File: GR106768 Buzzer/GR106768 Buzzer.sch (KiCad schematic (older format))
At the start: 0 parts

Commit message: Adding first pass at Buzzer Board schematic
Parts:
- added BZ1, BZ2: PKM33, symbol Device:Buzzer
- added C1: 47pF, symbol c_network:C_NETWORK
- added C10, C11, C30, C5, C7, C8, C9: 100nF, symbol Device:C
- added C12: 470μF, symbol Device:CP
- added C13, C14: 33nF, symbol Device:C
- added C2: 220pF, symbol Device:C
- added C3: 10nF, symbol Device:C
- added C4, C6: 680pF, symbol Device:C
- added D1: NC, symbol Device:D_Zener
- added D2: BAT54C, Package_TO_SOT_SMD:SOT-23, symbol Diode:BAT54C
- added D3, D4: BAT54S, Package_TO_SOT_SMD:SOT-23, symbol Diode:BAT54S
- added D5: BZX84C2V7, symbol Device:D_Zener
- added F1: 500mA, symbol Device:Fuse
- added FI1: BLA31BD221SN4D, FB_BLA31BD221SN4D, symbol bla31bd:BLA31BD221SN4D
- added J1: Conn_01x07, symbol Connector_Generic:Conn_01x07
- added L1: Core_Ferrite, symbol Device:L_Core_Ferrite
- added Q1, Q2: BC847, Package_TO_SOT_SMD:SOT-23, symbol Transistor_BJT:BC847
- added Q3, Q4: BC857, Package_TO_SOT_SMD:SOT-23, symbol Transistor_BJT:BC857
- added R1, R10, R2, R24, R29, R3, R59: 100k, symbol Device:R
- added R11: 105k, symbol Device:R
- added R12, R22: 470, symbol Device:R
- added R13, R14, R19, R20: 1.5, symbol Device:R
- added R15: 33, symbol Device:R
- added R16, R17, R4, R5: 10k, symbol Device:R
- added R18, R21: 150k, symbol Device:R
- added R23: 2.2K, symbol Device:R
- added R25: NC, symbol Device:R
- added R26: 137k, symbol Device:R
- added R27: 68k, symbol Device:R
- added R28, R9: 32.4k, symbol Device:R
- added R6: 50k, symbol Device:R
- added R69: 200k, symbol Device:R
- added R7: 51.1k, symbol Device:R
- added R8: 1k, symbol Device:R
- added U1, U2: MC33172, symbol Amplifier_Operational:LM358
- added U3: LMC7211, symbol lmc7211:LMC7211
- added U4: LMV321, symbol Amplifier_Operational:LMV321
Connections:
- net labels added: +12V, +5V, -12V, BUZ_ACT, GND, INHIB_STOP_INV, STOP_INV, SUPPLY_BUZ, TESTBUZ, TEST_BUZZER, VBAT, VCHARG
- wire segments 0 -> 244
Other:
- note added: "+5V_CPU"
- note added: "GND"
- note added: "INHIB-STOP-INV-CPU"
- note added: "PWM-BUZZER-CPU"
- note added: "STOP-INV-CPU"
- note added: "SUPPLY-BUZ-CPU"
- note added: "TEST-BUZZER-CPU"

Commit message: Changed global nets to hierarchical
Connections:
- net labels removed: TESTBUZ
- wire segments 244 -> 250
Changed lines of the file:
@@
 EESchema Schematic File Version 4
-LIBS:GR106768 Buzzer-cache
 EELAYER 30 0
 EELAYER END
@@
 	1    0    0    -1
 $EndComp
-Text GLabel 4700 4250 0    50   Input ~ 0
-SUPPLY_BUZ
 $Comp
 L Device:C C10
@@
 	0    -1   -1   0
 $EndComp
-Text GLabel 4325 2600 2    50   Input ~ 0
-TEST_BUZZER
-Text GLabel 4325 2750 2    50   Output ~ 0
-STOP_INV
 $Comp
 L Diode:BAT54S D4
@@
 	1    0    0    -1
 $EndComp
-Text GLabel 14525 6200 2    50   Output ~ 0
-TESTBUZ
-Text GLabel 12775 6975 0    50   Input ~ 0
-VBAT
-Text GLabel 12600 6075 0    50   Output ~ 0
-BUZ_ACT
 $Comp
 L Device:C C30
@@
 Wire Wire Line
 	13300 6975 13300 7050
-Text GLabel 13925 6975 2    50   Input ~ 0
-VCHARG
 Wire Wire Line
 	13925 6975 13700 6975
@@
 Wire Wire Line
 	2350 2800 2300 2800
-Text GLabel 4325 2450 2    50   Output ~ 0
-INHIB_STOP_INV
 Wire Wire Line
 	3175 2300 4325 2300
-Text GLabel 4325 2300 2    50   Input ~ 0
-SUPPLY_BUZ
 Wire Wire Line
 	6425 2900 5950 2900
@@
 Wire Wire Line
 	3750 6250 3750 6350
-$Sheet
-S 2450 7725 1200 900
-U 5E89C6B8
-F0 "GR106768_buzzer_charger" 50
-F1 "GR106768_buzzer_charger.sch" 50
-$EndSheet
 Wire Wire Line
 	7900 4450 13950 4450
@@
 	4250 2900 5025 2900
 Connection ~ 5025 2900
+Wire Wire Line
+	3650 7925 3825 7925
+Text HLabel 3825 7925 2    50   Output ~ 0
+SUPPLY_BUZ
+$Sheet
+S 2450 7725 1200 900
+U 5E89C6B8
+F0 "GR106768_buzzer_charger" 50
+F1 "GR106768_buzzer_charger.sch" 50
+F2 "BUZ_ACT" I L 2450 7925 50
+F3 "SUPPLY_BUZ" O R 3650 7925 50
+F4 "STOP_INV" I L 2450 8025 50
+F5 "INHIB_STOP_INV" I L 2450 8125 50
+F6 "VBAT" O R 3650 8025 50
+F7 "VCHARG" O R 3650 8125 50
+$EndSheet
+Wire Wire Line
+	2300 8125 2450 8125
+Wire Wire Line
+	2300 8025 2450 8025
+Wire Wire Line
+	2300 7925 2450 7925
+Text HLabel 2300 7925 0    50   Input ~ 0
+BUZ_ACT
+Text HLabel 2300 8025 0    50   Input ~ 0
+STOP_INV
+Text HLabel 2300 8125 0    50   Input ~ 0
+INHIB_STOP_INV
+Text HLabel 3825 8125 2    50   Output ~ 0
+VCHARG
+Wire Wire Line
+	3650 8025 3825 8025
+Text HLabel 3825 8025 2    50   Output ~ 0
+VBAT
+Text HLabel 12775 6975 0    50   Input ~ 0
+VBAT
+Text HLabel 12600 6075 0    50   Output ~ 0
+BUZ_ACT
+Text HLabel 4700 4250 0    50   Input ~ 0
+SUPPLY_BUZ
+Text HLabel 4325 2750 2    50   Output ~ 0
+STOP_INV
+Text HLabel 14525 6200 2    50   Output ~ 0
+TEST_BUZZER
+Text HLabel 4325 2600 2    50   Input ~ 0
+TEST_BUZZER
+Text HLabel 4325 2450 2    50   Output ~ 0
+INHIB_STOP_INV
+Text HLabel 4325 2300 2    50   Input ~ 0
+SUPPLY_BUZ
+Wire Wire Line
+	3650 8125 3825 8125
+Text HLabel 13925 6975 2    50   Input ~ 0
+VCHARG
 $EndSCHEMATC

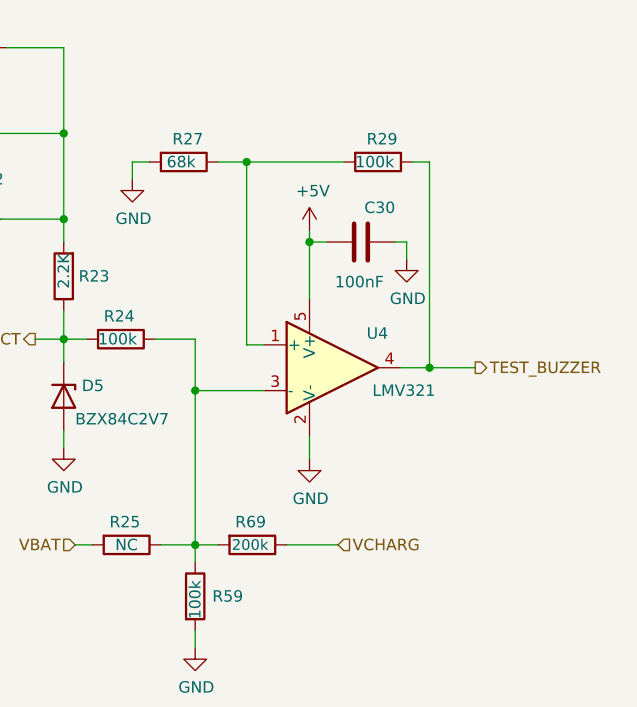
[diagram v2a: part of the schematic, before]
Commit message: Fixed U4 pins (KiCad part is different)
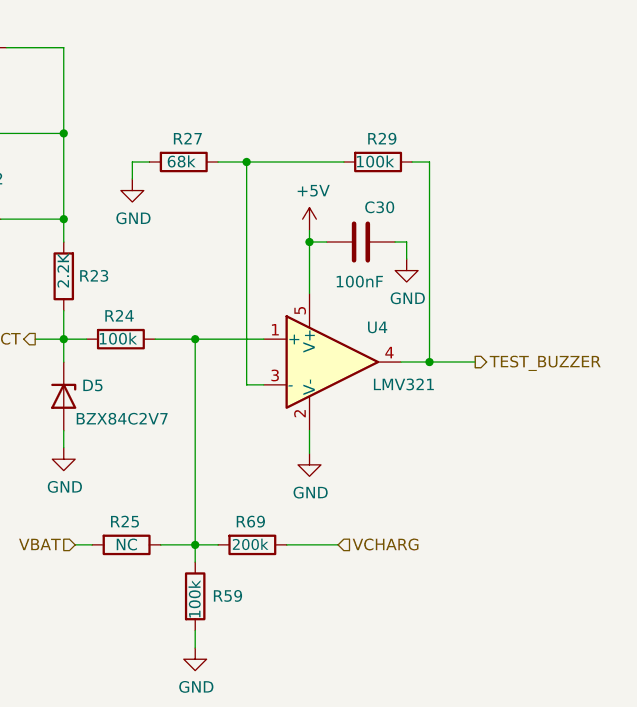
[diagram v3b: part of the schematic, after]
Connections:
- wire segments 250 -> 249
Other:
- moved on the sheet: U4
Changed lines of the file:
@@
 	10400 3325 10400 3125
-$Comp
-L Amplifier_Operational:LMV321 U4
-U 1 1 5E9F6105
-P 13900 6200
-F 0 "U4" H 14050 6350 50  0000 L CNN
-F 1 "LMV321" H 14075 6100 50  0000 L CNN
-F 2 "" H 13900 6200 50  0001 L CNN
-F 3 "http://www.ti.com/lit/ds/symlink/lmv324.pdf" H 13900 6200 50  0001 C CNN
-	1    13900 6200
-	1    0    0    -1
-$EndComp
-$Comp
-L power:GND #PWR027
-U 1 1 5E9F8A01
-P 13800 6600
-F 0 "#PWR027" H 13800 6350 50  0001 C CNN
-F 1 "GND" H 13805 6427 50  0000 C CNN
-F 2 "" H 13800 6600 50  0001 C CNN
-F 3 "" H 13800 6600 50  0001 C CNN
-	1    13800 6600
-	1    0    0    -1
-$EndComp
 $Comp
 L Device:C C30
@@
 $EndComp
 $Comp
-L power:GND #PWR021
-U 1 1 5EA0E815
-P 14225 5725
-F 0 "#PWR021" H 14225 5475 50  0001 C CNN
-F 1 "GND" H 14230 5552 50  0000 C CNN
-F 2 "" H 14225 5725 50  0001 C CNN
-F 3 "" H 14225 5725 50  0001 C CNN
-	1    14225 5725
-	1    0    0    -1
-$EndComp
-$Comp
 L Device:R R69
 U 1 1 5EA111CA
@@
 $EndComp
 Wire Wire Line
-	14200 6200 14325 6200
-Wire Wire Line
 	13875 5650 13800 5650
 Wire Wire Line
-	13800 5650 13800 5900
-Wire Wire Line
 	14175 5650 14225 5650
-Wire Wire Line
-	14225 5650 14225 5725
 $Comp
 L power:+5V #PWR018
@@
 $EndComp
 Wire Wire Line
-	13800 5600 13800 5650
-Connection ~ 13800 5650
-Wire Wire Line
-	14325 5300 14325 6200
-Connection ~ 14325 6200
-Wire Wire Line
-	14325 6200 14525 6200
-Wire Wire Line
 	14250 5300 14325 5300
 Wire Wire Line
 	13950 5300 13525 5300
-Wire Wire Line
-	13600 6100 13525 6100
-Wire Wire Line
-	13525 6100 13525 5300
 Connection ~ 13525 5300
 Wire Wire Line
@@
 Wire Wire Line
 	13025 5300 13025 5375
-Wire Wire Line
-	13800 6600 13800 6500
 Wire Wire Line
 	12775 6975 12850 6975
@@
 Connection ~ 13300 6975
 Wire Wire Line
-	13600 6300 13300 6300
-Wire Wire Line
-	13300 6300 13300 6975
-Wire Wire Line
 	13125 6075 13300 6075
-Wire Wire Line
-	13300 6075 13300 6300
-Connection ~ 13300 6300
 $Comp
 L power:GND #PWR026
@@
 Text HLabel 4325 2750 2    50   Output ~ 0
 STOP_INV
-Text HLabel 14525 6200 2    50   Output ~ 0
-TEST_BUZZER
 Text HLabel 4325 2600 2    50   Input ~ 0
 TEST_BUZZER
@@
 Text HLabel 13925 6975 2    50   Input ~ 0
 VCHARG
+Wire Wire Line
+	14225 5650 14225 5725
+Text HLabel 14525 6175 2    50   Output ~ 0
+TEST_BUZZER
+Wire Wire Line
+	13800 6575 13800 6475
+Wire Wire Line
+	14325 5300 14325 6175
+$Comp
+L power:GND #PWR021
+U 1 1 5EA0E815
+P 14225 5725
+F 0 "#PWR021" H 14225 5475 50  0001 C CNN
+F 1 "GND" H 14230 5552 50  0000 C CNN
+F 2 "" H 14225 5725 50  0001 C CNN
+F 3 "" H 14225 5725 50  0001 C CNN
+	1    14225 5725
+	1    0    0    -1
+$EndComp
+$Comp
+L power:GND #PWR027
+U 1 1 5E9F8A01
+P 13800 6575
+F 0 "#PWR027" H 13800 6325 50  0001 C CNN
+F 1 "GND" H 13805 6402 50  0000 C CNN
+F 2 "" H 13800 6575 50  0001 C CNN
+F 3 "" H 13800 6575 50  0001 C CNN
+	1    13800 6575
+	1    0    0    -1
+$EndComp
+$Comp
+L Amplifier_Operational:LMV321 U4
+U 1 1 5E9F6105
+P 13900 6175
+F 0 "U4" H 14050 6325 50  0000 L CNN
+F 1 "LMV321" H 14075 6075 50  0000 L CNN
+F 2 "" H 13900 6175 50  0001 L CNN
+F 3 "http://www.ti.com/lit/ds/symlink/lmv324.pdf" H 13900 6175 50  0001 C CNN
+	1    13900 6175
+	1    0    0    -1
+$EndComp
+Wire Wire Line
+	13300 6075 13300 6975
+Wire Wire Line
+	13300 6075 13600 6075
+Connection ~ 13300 6075
+Wire Wire Line
+	13525 6275 13600 6275
+Wire Wire Line
+	13525 5300 13525 6275
+Wire Wire Line
+	13800 5600 13800 5650
+Wire Wire Line
+	13800 5875 13800 5650
+Connection ~ 13800 5650
+Connection ~ 14325 6175
+Wire Wire Line
+	14325 6175 14525 6175
+Wire Wire Line
+	14200 6175 14325 6175
 $EndSCHEMATC

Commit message: Merged Buzzer libraries into master library
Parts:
- removed C1: 47pF, symbol c_network:C_NETWORK
- removed FI1: BLA31BD221SN4D, FB_BLA31BD221SN4D, symbol bla31bd:BLA31BD221SN4D
- removed U3: LMC7211, symbol lmc7211:LMC7211
- added C1: 47pF, symbol GR106768~Buzzer:C_NETWORK
- added FI1: BLA31BD221SN4D, FB_BLA31BD221SN4D, symbol GR106768~Buzzer:BLA31BD221SN4D
- added U3: LMC7211, symbol GR106768~Buzzer:LMC7211
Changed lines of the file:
@@
-$EndComp
-$Comp
-L lmc7211:LMC7211 U3
-U 1 1 5E8BBAEB
-P 5900 4850
-F 0 "U3" H 5950 5150 50  0000 L CNN
-F 1 "LMC7211" H 5950 4575 50  0000 L CNN
-F 2 "" H 5700 4850 50  0001 C CNN
-F 3 "" H 5700 4850 50  0001 C CNN
-	1    5900 4850
-	1    0    0    -1
 $EndComp
 $Comp
@@
 Wire Wire Line
 	8950 3500 9175 3500
-$Comp
-L bla31bd:BLA31BD221SN4D FI1
-U 1 1 5E8BD79C
-P 3950 2700
-F 0 "FI1" H 3950 3175 50  0000 C CNN
-F 1 "BLA31BD221SN4D" H 3950 2325 50  0000 C CNN
-F 2 "FB_BLA31BD221SN4D" H 3950 2700 50  0001 L BNN
-F 3 "1206 Murata" H 3950 2700 50  0001 L BNN
-F 4 "1mm" H 3950 2700 50  0001 L BNN "Champ4"
-F 5 "Murata Electronics" H 3950 2700 50  0001 L BNN "Champ5"
-F 6 "None" H 3950 2700 50  0001 L BNN "Champ6"
-F 7 "Manufacturer recommendations" H 3950 2700 50  0001 L BNN "Champ7"
-F 8 "Unavailable" H 3950 2700 50  0001 L BNN "Champ8"
-F 9 "Ferrite Beads Chip Bead Array 1KOhm 25% 100MHz 50mA 1206 Paper T/R" H 3950 2700 50  0001 L BNN "Champ9"
-F 10 "JENF243A–0008N-01" H 3950 2700 50  0001 L BNN "Champ10"
-F 11 "BLA31AG102SN4D" H 3950 2700 50  0001 L BNN "Champ11"
-	1    3950 2700
-	1    0    0    -1
-$EndComp
 Wire Wire Line
 	4250 2600 4325 2600
@@
 Wire Wire Line
 	3125 2500 3125 2750
-$Comp
-L c_network:C_NETWORK C1
-U 1 1 5E8870D5
-P 3225 4000
-F 0 "C1" H 3625 4175 50  0000 L CNN
-F 1 "47pF" H 3625 3825 50  0000 L CNN
-F 2 "" H 2963 3850 50  0001 C CNN
-F 3 "~" H 2925 4000 50  0001 C CNN
-	1    3225 4000
-	1    0    0    -1
-$EndComp
 Wire Wire Line
 	2925 2900 2925 3800
@@
 Wire Wire Line
 	14200 6175 14325 6175
+$Comp
+L GR106768~Buzzer:BLA31BD221SN4D FI1
+U 1 1 5FB00CBD
+P 3950 2700
+F 0 "FI1" H 3950 3150 50  0000 C CNN
+F 1 "BLA31BD221SN4D" H 3950 2350 50  0000 C CNN
+F 2 "FB_BLA31BD221SN4D" H 3550 2200 50  0001 L BNN
+F 3 "1206 Murata" H 3650 1650 50  0001 L BNN
+F 4 "Murata Electronics" H 3600 2100 50  0001 L BNN "Champ5"
+	1    3950 2700
+	1    0    0    -1
+$EndComp
+$Comp
+L GR106768~Buzzer:C_NETWORK C1
+U 1 1 5FB0366D
+P 3225 4000
+F 0 "C1" H 3678 4059 50  0000 L CNN
+F 1 "47pF" H 3678 3968 50  0000 L CNN
+F 2 "" H 2963 3850 50  0001 C CNN
+F 3 "~" H 2925 4000 50  0001 C CNN
+	1    3225 4000
+	1    0    0    -1
+$EndComp
+$Comp
+L GR106768~Buzzer:LMC7211 U3
+U 1 1 5FB0685F
+P 5900 4850
+F 0 "U3" H 5975 5100 50  0000 L CNN
+F 1 "LMC7211" H 5975 4575 50  0000 L CNN
+F 2 "" H 5700 4850 50  0001 C CNN
+F 3 "" H 5700 4850 50  0001 C CNN
+	1    5900 4850
+	1    0    0    -1
+$EndComp
 $EndSCHEMATC

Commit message: Updating Buzzer and start of board
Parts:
- BZ1, BZ2: footprint (none) -> footprint_buzzer:Buzzer_Murata_PKM33EPH1201C
- C1: footprint (none) -> footprint_buzzer:CA0612KRX7R9BB102
- C10, C11, C12, C13, C14, C2, C3, C30, C4, C5, C6, C7, C8, C9: footprint (none) -> Capacitor_SMD:C_0402_1005Metric
- D1: footprint (none) -> footprint_buzzer:DIO_MBRM110LT1G
- D5: footprint (none) -> Diode_SMD:D_SOT-23_ANK
- F1: footprint (none) -> footprint_buzzer:Fuse_Littlefuse-0451_500MRL
- FI1: footprint FB_BLA31BD221SN4D -> footprint_buzzer:FB_BLA31BD221SN4D
- IC1: renamed from U3; footprint (none) -> Package_TO_SOT_SMD:SOT-23-5
- IC2: renamed from U2; footprint (none) -> Package_SO:PowerIntegrations_SO-8
- IC3: renamed from U1; footprint (none) -> Package_SO:PowerIntegrations_SO-8
- IC4: renamed from U4; footprint (none) -> Package_TO_SOT_SMD:SOT-23-5
- J1: footprint (none) -> TerminalBlock_4Ucon:TerminalBlock_4Ucon_1x07_P3.50mm_Horizontal
- L1: footprint (none) -> Inductor_SMD:L_1206_3216Metric_Pad1.42x1.75mm_HandSolder
- R1, R10, R11, R12, R13, R14, R15, R16, R17, R18, R19, R2, R20, R21, R22, R23, R24, R25, R26, R27, R28, R29, R3, R4, R5, R59, R6, R69, R7, R8, R9: footprint (none) -> Resistor_SMD:R_0402_1005Metric
- renumbered Q1 to T1, Q3 to T2, Q2 to T3, Q4 to T4
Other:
- note added: "FARNELL : 156711"

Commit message: Merging Buzzer schematic
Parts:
- C12: footprint Capacitor_SMD:C_0402_1005Metric -> Capacitor_THT:CP_Axial_L25.0mm_D10.0mm_P30.00mm_Horizontal
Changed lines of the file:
@@
 F 0 "C12" H 11375 3400 50  0000 L CNN
 F 1 "470μF" H 11100 3150 50  0000 L CNN
-F 2 "Capacitor_SMD:C_0402_1005Metric" H 11388 3125 50  0001 C CNN
+F 2 "Capacitor_THT:CP_Axial_L25.0mm_D10.0mm_P30.00mm_Horizontal" H 11388 3125 50  0001 C CNN
 F 3 "~" H 11350 3275 50  0001 C CNN
 	1    11350 3275

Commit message: Associating Buzzer symbols/footprints
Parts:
- BUZ1: renamed from BZ1; footprint footprint_buzzer:Buzzer_Murata_PKM33EPH1201C -> footprint_buzzer:PKM33EPH-1201C_1
- BUZ2: renamed from BZ2; footprint footprint_buzzer:Buzzer_Murata_PKM33EPH1201C -> footprint_buzzer:PKM33EPH-1201C_1
- C1: symbol GR106768~Buzzer:C_NETWORK -> GR106768_Buzzer:C_NETWORK
- FI1: symbol GR106768~Buzzer:BLA31BD221SN4D -> GR106768_Buzzer:BLA31BD221SN4D
- IC1: symbol GR106768~Buzzer:LMC7211 -> GR106768_Buzzer:LMC7211
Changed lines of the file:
@@
 EESchema Schematic File Version 4
-LIBS:GR106768 Buzzer-cache
 EELAYER 30 0
 EELAYER END
@@
 $EndComp
 $Comp
-L Device:Buzzer BZ1
+L Device:Buzzer BUZ1
 U 1 1 5E89A28C
 P 9975 2575
-F 0 "BZ1" V 10225 2650 50  0000 R CNN
+F 0 "BUZ1" V 10225 2650 50  0000 R CNN
 F 1 "PKM33" V 10150 2700 50  0000 R CNN
-F 2 "footprint_buzzer:Buzzer_Murata_PKM33EPH1201C" V 9950 2675 50  0001 C CNN
+F 2 "footprint_buzzer:PKM33EPH-1201C_1" V 9950 2675 50  0001 C CNN
 F 3 "~" V 9950 2675 50  0001 C CNN
 	1    9975 2575
@@
 $EndComp
 $Comp
-L Device:Buzzer BZ2
+L Device:Buzzer BUZ2
 U 1 1 5E89B391
 P 9975 3075
-F 0 "BZ2" V 10150 3000 50  0000 L CNN
+F 0 "BUZ2" V 10150 3000 50  0000 L CNN
 F 1 "PKM33" V 10225 2950 50  0000 L CNN
-F 2 "footprint_buzzer:Buzzer_Murata_PKM33EPH1201C" V 9950 3175 50  0001 C CNN
+F 2 "footprint_buzzer:PKM33EPH-1201C_1" V 9950 3175 50  0001 C CNN
 F 3 "~" V 9950 3175 50  0001 C CNN
 	1    9975 3075
@@
 	14200 6175 14325 6175
 $Comp
-L GR106768~Buzzer:BLA31BD221SN4D FI1
+L GR106768_Buzzer:BLA31BD221SN4D FI1
 U 1 1 5FB00CBD
 P 3950 2700
@@
 $EndComp
 $Comp
-L GR106768~Buzzer:C_NETWORK C1
+L GR106768_Buzzer:C_NETWORK C1
 U 1 1 5FB0366D
 P 3225 4000
@@
 $EndComp
 $Comp
-L GR106768~Buzzer:LMC7211 IC1
+L GR106768_Buzzer:LMC7211 IC1
 U 1 1 5FB0685F
 P 5900 4850
